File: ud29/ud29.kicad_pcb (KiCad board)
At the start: 2 copper layers, 97.5 x 97.5 mm, 123 parts, among them J1 Conn_01x02, J10 Conn_01x01, J11 Conn_01x01, J12 Conn_01x01, J13 Conn_01x01, J14 Conn_01x02, J15 Conn_01x03, J16 Conn_01x02, J17 Conn_01x02, J18 Conn_01x02, J19 Conn_01x02, J2 Conn_01x02, J3 Conn_01x02, J4 Conn_01x02, J5 Conn_01x02, J6 Conn_02x03_Odd_Even, J7 Conn_01x02, J8 Conn_01x02, J9 Conn_01x03, Q1 IRF9540N, Q2 IRF540N, Q3 IRF9540N, Q4 IRF540N, Q5 2N3906, U1 LM7824_TO220, U15 MC34164, U2 LM7812_TO220, U3 LM7805_TO220, U4 TL3116, U5 74HC08, U6 LM311, U7 74HC74, U8 74HC14, U9 UCC27243

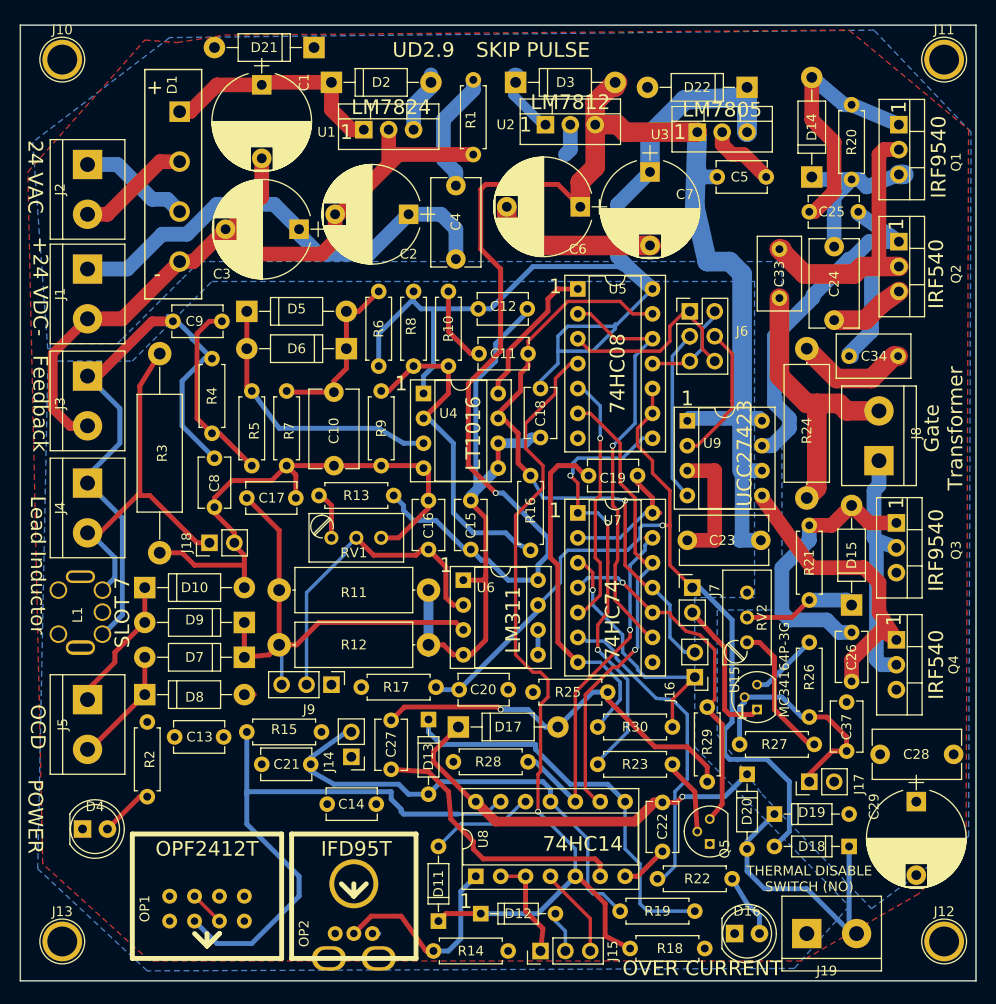
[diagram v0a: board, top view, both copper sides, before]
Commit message: kicad update 6.0.11
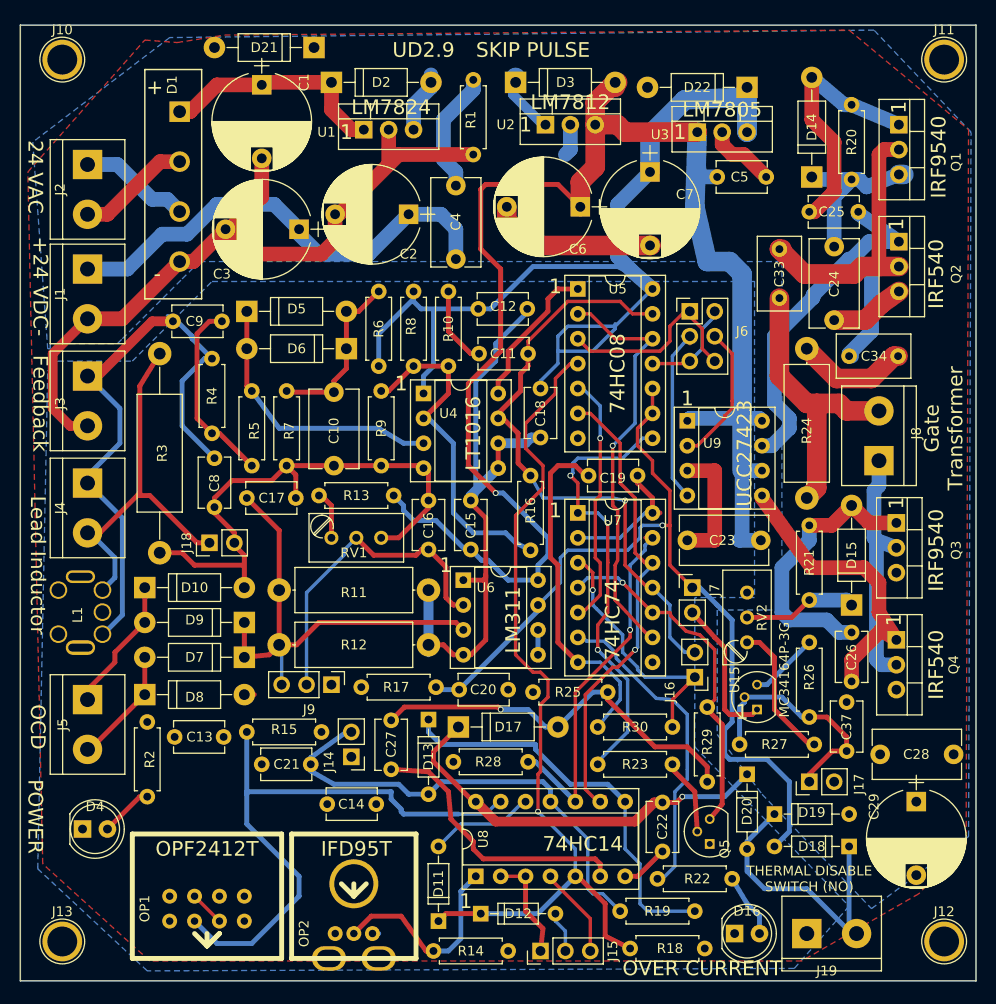
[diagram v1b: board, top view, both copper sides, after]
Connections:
- C27 pad 2: Net-(C27-Pad2) -> (no net)
- D17 pad 2: Net-(C27-Pad2) -> (no net)
- R25 pad 1: Net-(C27-Pad2) -> (no net)
- R29 pad 2: Net-(C27-Pad2) -> (no net)
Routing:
- net Net-(C27-Pad2): track 41.3 -> 0.00 mm, vias 1 -> 0
- net (no net): track 0.00 -> 41.3 mm, vias 0 -> 1
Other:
- net class Default removed
